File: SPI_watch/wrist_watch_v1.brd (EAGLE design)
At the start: 34.3 x 33.7 mm, 30 parts

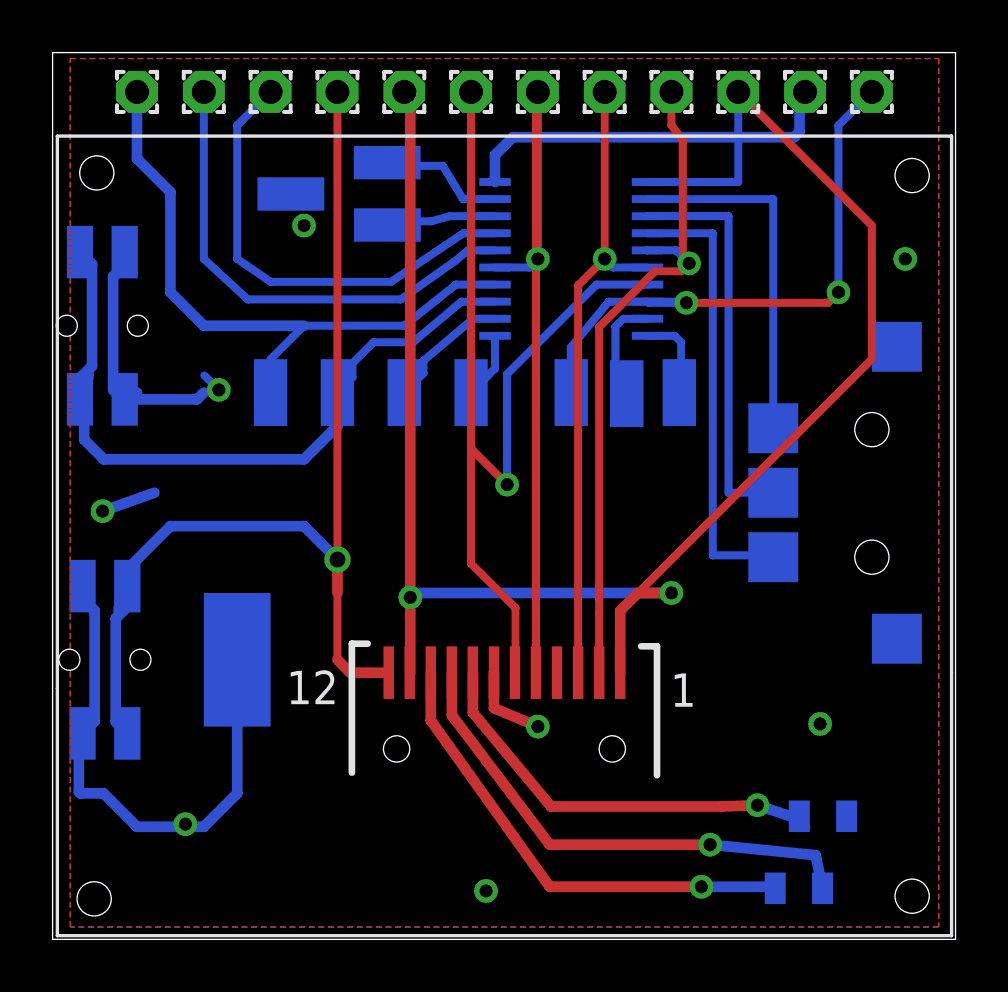
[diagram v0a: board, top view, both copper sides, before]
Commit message: Added SPI LCD Displays
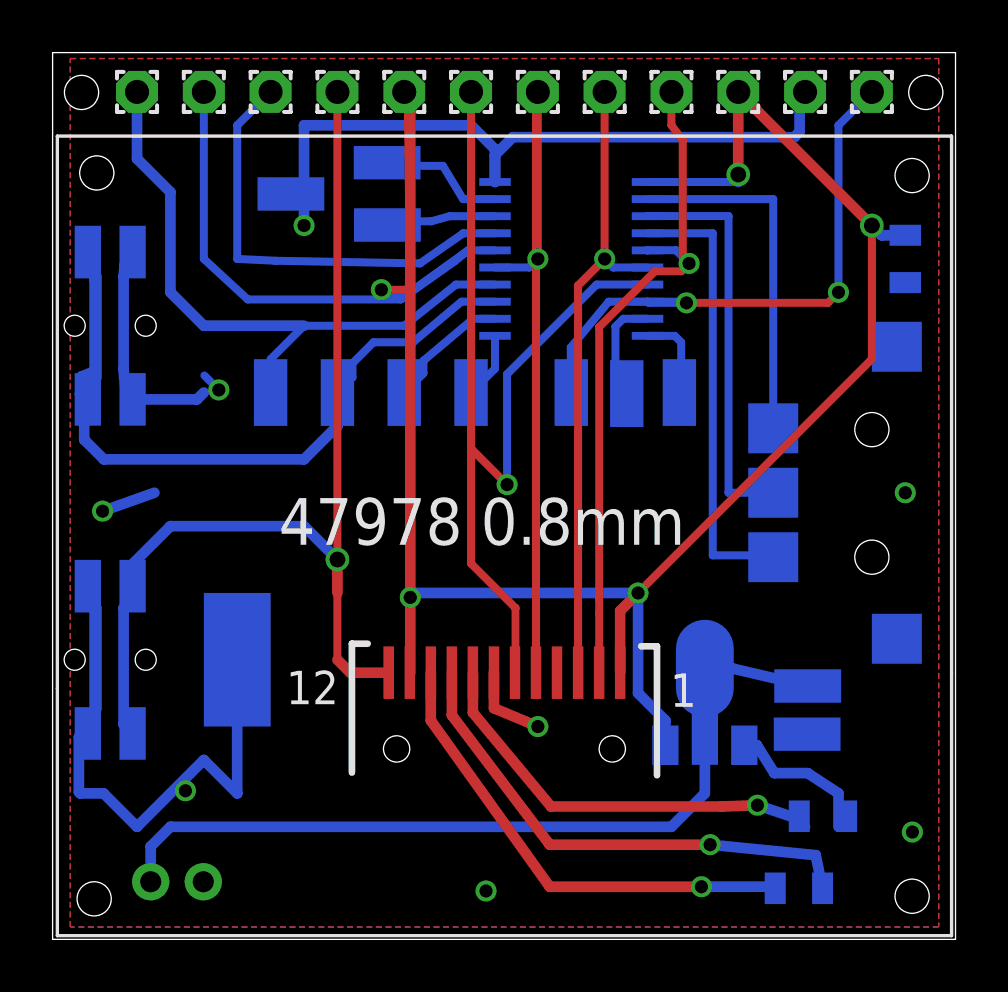
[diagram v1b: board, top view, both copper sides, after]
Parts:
- added C3: (no value), SparkFun-Passives:0805
- added CN1: (no value), adafruit:JST-PH-2-THM-RA
- added GND3, VIN: (no value), wirepad:SMD1,27-2,54
- added IC1: MCP170312MB, linear:SOT89
- moved U$4 0.30 mm to (2.84, 24.1)
- moved U$2 0.20 mm to (2.74, 11.4)
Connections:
- removed net N$11: MSP430.16, RST.1
- new net N$23: CN1.1, IC1.2@1, VIN.1
- net GND: now also C3.1, CN1.2, GND3.1, IC1.1
- net VDD: now also C3.2, IC1.3, MSP430.16, RST.1
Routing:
- net VDD: track 68.5 -> 105.1 mm, vias 2 -> 5
- net N$23: track 0.00 -> 32.0 mm
- net GND: track 50.8 -> 70.1 mm
- net N$11: track 18.6 -> 0.00 mm
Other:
- board text added: "47978 0.8mm"
- board text removed: "GND"
